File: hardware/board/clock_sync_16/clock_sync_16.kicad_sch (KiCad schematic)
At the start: 1 part, among them U21 SN74LVC1G125DCK

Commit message: route pcb v0.1
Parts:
- added C10: 1uF, Capacitor_SMD:C_0402_1005Metric, symbol Device:C
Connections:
- net +3.3V: now also C10.1
- net GND: now also C10.2
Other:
- note removed: "TODO: Ephys "slow uart" output. TODO: 32.768KHz crystal."
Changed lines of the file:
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@@
     (company "The Allen Institute")
   )
+  (wire (pts (xy 140.335 189.23) (xy 140.335 190.5))
+    (stroke (width 0) (type default))
+  )
   (wire (pts (xy 155.575 48.26) (xy 156.845 48.26))
     (stroke (width 0) (type default))
@@
     (stroke (width 0) (type default))
   )
+  (wire (pts (xy 140.335 180.34) (xy 140.335 181.61))
+    (stroke (width 0) (type default))
+  )
   (wire (pts (xy 142.875 36.83) (xy 142.875 38.1))
     (stroke (width 0) (type default))
@@
   (wire (pts (xy 105.41 76.2) (xy 181.61 76.2))
     (stroke (width 0) (type default))
-  )
-  (text "TODO: Ephys \"slow uart\" output.\nTODO: 32.768KHz crystal."
-    (at 123.19 146.685 0)
-    (effects (font (size 2 2) (thickness 0.4) bold) (justify left bottom))
   )
   (global_label "HARP_CLKOUT" (shape input) (at 156.845 48.26 0) (fields_autoplaced)
@@
     )
   )
+  (symbol (lib_id "Device:C") (at 140.335 185.42 0) (unit 1)
+    (in_bom yes) (on_board yes) (dnp no)
+    (property "Reference" "C10" (at 140.335 182.88 0)
+      (effects (font (size 1.27 1.27)) (justify left))
+    )
+    (property "Value" "1uF" (at 141.605 187.96 0)
+      (effects (font (size 1.27 1.27)) (justify left))
+    )
+    (property "Footprint" "Capacitor_SMD:C_0402_1005Metric" (at 141.3002 189.23 0)
+      (effects (font (size 1.27 1.27)) hide)
+    )
+    (property "Datasheet" "https://search.murata.co.jp/Ceramy/image/img/A01X/G101/ENG/GRM155R6YA105KE11-01.pdf" (at 140.335 185.42 0)
+      (effects (font (size 1.27 1.27)) hide)
+    )
+    (property "Notes" "must not be polarized" (at 140.335 185.42 0)
+      (effects (font (size 1.27 1.27)) hide)
+    )
+    (property "Link" "https://www.digikey.com/en/products/detail/murata-electronics/GRM155R6YA105KE11J/4905163" (at 140.335 185.42 0)
+      (effects (font (size 1.27 1.27)) hide)
+    )
+    (property "Manufacturer Number" "GRM155R6YA105KE11J" (at 140.335 185.42 0)
+      (effects (font (size 1.27 1.27)) hide)
+    )
+    (property "Manufacturer" "Murata Electronics" (at 140.335 185.42 0)
+      (effects (font (size 1.27 1.27)) hide)
+    )
+    (property "Rated Voltage" "35V" (at 140.335 185.42 0)
+      (effects (font (size 1.27 1.27)) hide)
+    )
+    (property "Temperature Coefficient" "X5R" (at 140.335 185.42 0)
+      (effects (font (size 1.27 1.27)) hide)
+    )
+    (property "PCBWay Link" "" (at 140.335 185.42 0)
+      (effects (font (size 1.27 1.27)) hide)
+    )
+    (pin "1")
+    (pin "2")
+    (instances
+      (project "clock_sync_16"
+        (path "/8fe3245e-7a82-4862-8bfd-ddbb03ffdc18/ba147b73-594a-4106-8069-105093132ec6"
+          (reference "C10") (unit 1)
+        )
+        (path "/8fe3245e-7a82-4862-8bfd-ddbb03ffdc18"
+          (reference "C54") (unit 1)
+        )
+      )
+      (project "harp_lick_detector_capactive"
+        (path "/e63e39d7-6ac0-4ffd-8aa3-1841a4541b55/eb8325ca-9747-4676-8e08-1fb825a7219f"
+          (reference "C8") (unit 1)
+        )
+      )
+    )
+  )
+  (symbol (lib_id "power:+3.3V") (at 140.335 180.34 0) (unit 1)
+    (in_bom yes) (on_board yes) (dnp no)
+    (property "Reference" "#PWR09" (at 140.335 184.15 0)
+      (effects (font (size 1.27 1.27)) hide)
+    )
+    (property "Value" "+3.3V" (at 140.335 176.53 0)
+      (effects (font (size 1.27 1.27)))
+    )
+    (property "Footprint" "" (at 140.335 180.34 0)
+      (effects (font (size 1.27 1.27)) hide)
+    )
+    (property "Datasheet" "" (at 140.335 180.34 0)
+      (effects (font (size 1.27 1.27)) hide)
+    )
+    (pin "1")
+    (instances
+      (project "clock_sync_16"
+        (path "/8fe3245e-7a82-4862-8bfd-ddbb03ffdc18/ba147b73-594a-4106-8069-105093132ec6"
+          (reference "#PWR09") (unit 1)
+        )
+        (path "/8fe3245e-7a82-4862-8bfd-ddbb03ffdc18"
+          (reference "#PWR037") (unit 1)
+        )
+      )
+    )
+  )
   (symbol (lib_id "74xGxx:SN74LVC1G125DCK") (at 142.875 48.26 0) (unit 1)
     (in_bom yes) (on_board yes) (dnp no)
@@
     )
   )
-  (symbol (lib_name "+3.3V_1") (lib_id "power:+3.3V") (at 137.795 36.83 0) (unit 1)
+  (symbol (lib_id "power:GND") (at 140.335 190.5 0) (unit 1)
+    (in_bom yes) (on_board yes) (dnp no)
+    (property "Reference" "#PWR058" (at 140.335 196.85 0)
+      (effects (font (size 1.27 1.27)) hide)
+    )
+    (property "Value" "GND" (at 140.335 194.31 0)
+      (effects (font (size 1.27 1.27)))
+    )
+    (property "Footprint" "" (at 140.335 190.5 0)
+      (effects (font (size 1.27 1.27)) hide)
+    )
+    (property "Datasheet" "" (at 140.335 190.5 0)
+      (effects (font (size 1.27 1.27)) hide)
+    )
+    (pin "1")
+    (instances
+      (project "clock_sync_16"
+        (path "/8fe3245e-7a82-4862-8bfd-ddbb03ffdc18"
+          (reference "#PWR058") (unit 1)
+        )
+      )
+    )
+  )
+  (symbol (lib_id "power:+3.3V") (at 137.795 36.83 0) (unit 1)
     (in_bom yes) (on_board yes) (dnp no)
     (property "Reference" "#PWR09" (at 137.795 40.64 0)

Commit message: draft v0.1 pcb
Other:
- note added: "Buffer Bypass Cap"
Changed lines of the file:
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@@
     (stroke (width 0) (type default))
+  )
+  (text "Buffer Bypass Cap" (at 133.35 173.355 0)
+    (effects (font (size 1.27 1.27)) (justify left bottom))
   )
   (global_label "HARP_CLKOUT" (shape input) (at 156.845 48.26 0) (fields_autoplaced)

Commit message: draft firmware
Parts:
- U21: Manufacturer (none) -> Texas Instruments; Manufacturer Number (none) -> SN74LVC1G125DCKR
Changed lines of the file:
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@@
+      (effects (font (size 1.27 1.27)) hide)
+    )
+    (property "Manufacturer" "Texas Instruments" (at 142.875 48.26 0)
+      (effects (font (size 1.27 1.27)) hide)
+    )
+    (property "Manufacturer Number" "SN74LVC1G125DCKR" (at 142.875 48.26 0)
       (effects (font (size 1.27 1.27)) hide)
     )

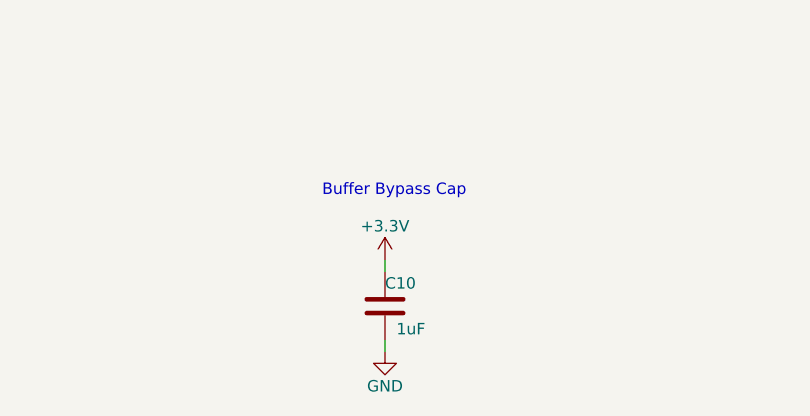
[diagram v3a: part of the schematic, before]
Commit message: add pps/slow_uart output options
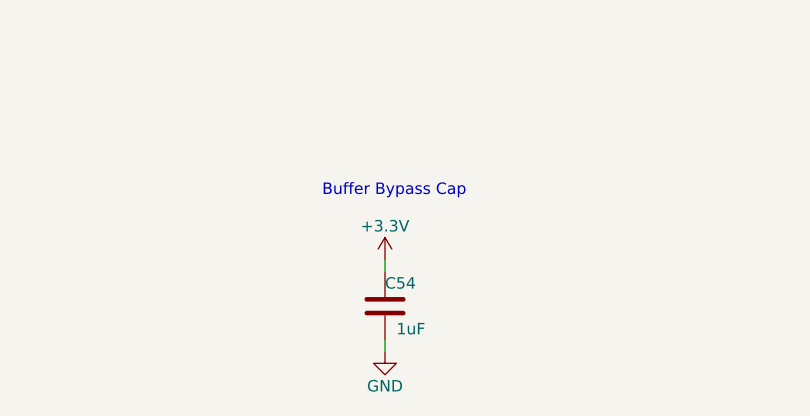
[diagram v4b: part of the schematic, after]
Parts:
- renumbered C10 to C54

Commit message: update harp core; update led resistors and deprecated parts; bump versions
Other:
- title: (none) -> harp.device.white-rabbit
- moved on the sheet: C54
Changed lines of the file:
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@@
 	(paper "A4")
 	(title_block
-		(rev "0.1")
+		(title "harp.device.white-rabbit")
+		(date "2025-02-21")
+		(rev "1.0.0")
 		(company "The Allen Institute")
 	)
 	(wire
 		(pts
-			(xy 140.335 189.23) (xy 140.335 190.5)
+			(xy 162.56 189.23) (xy 162.56 190.5)
 		)
 		(stroke
@@
 	(wire
 		(pts
-			(xy 140.335 180.34) (xy 140.335 181.61)
+			(xy 162.56 180.34) (xy 162.56 181.61)
 		)
 		(stroke
@@
 	(text "Buffer Bypass Cap"
 		(exclude_from_sim no)
-		(at 133.35 173.355 0)
+		(at 154.94 172.72 0)
 		(effects
 			(font
@@
 	(symbol
 		(lib_id "Device:C")
-		(at 140.335 185.42 0)
+		(at 162.56 185.42 0)
 		(unit 1)
 		(exclude_from_sim no)
@@
 		(dnp no)
 		(property "Reference" "C54"
-			(at 140.335 182.88 0)
+			(at 162.56 182.88 0)
 			(effects
 				(font
@@
 		)
 		(property "Value" "1uF"
-			(at 141.605 187.96 0)
+			(at 163.83 187.96 0)
 			(effects
 				(font
@@
 		)
 		(property "Footprint" "Capacitor_SMD:C_0402_1005Metric"
-			(at 141.3002 189.23 0)
+			(at 163.5252 189.23 0)
 			(effects
 				(font
@@
 		)
 		(property "Datasheet" "https://search.murata.co.jp/Ceramy/image/img/A01X/G101/ENG/GRM155R6YA105KE11-01.pdf"
-			(at 140.335 185.42 0)
+			(at 162.56 185.42 0)
 			(effects
 				(font
@@
 		)
 		(property "Description" ""
-			(at 140.335 185.42 0)
+			(at 162.56 185.42 0)
 			(effects
 				(font
@@
 		)
 		(property "Notes" "must not be polarized"
-			(at 140.335 185.42 0)
+			(at 162.56 185.42 0)
 			(effects
 				(font
@@
 		)
 		(property "Link" "https://www.digikey.com/en/products/detail/murata-electronics/GRM155R6YA105KE11J/4905163"
-			(at 140.335 185.42 0)
+			(at 162.56 185.42 0)
 			(effects
 				(font
@@
 		)
 		(property "Manufacturer Number" "GRM155R6YA105KE11J"
-			(at 140.335 185.42 0)
+			(at 162.56 185.42 0)
 			(effects
 				(font
@@
 		)
 		(property "Manufacturer" "Murata Electronics"
-			(at 140.335 185.42 0)
+			(at 162.56 185.42 0)
 			(effects
 				(font
@@
 		)
 		(property "Rated Voltage" "35V"
-			(at 140.335 185.42 0)
+			(at 162.56 185.42 0)
 			(effects
 				(font
@@
 		)
 		(property "Temperature Coefficient" "X5R"
-			(at 140.335 185.42 0)
+			(at 162.56 185.42 0)
 			(effects
 				(font
@@
 		)
 		(property "PCBWay Link" ""
-			(at 140.335 185.42 0)
+			(at 162.56 185.42 0)
 			(effects
 				(font
@@
 	(symbol
 		(lib_id "power:+3.3V")
-		(at 140.335 180.34 0)
+		(at 162.56 180.34 0)
 		(unit 1)
 		(exclude_from_sim no)
@@
 		(dnp no)
 		(property "Reference" "#PWR037"
-			(at 140.335 184.15 0)
+			(at 162.56 184.15 0)
 			(effects
 				(font
@@
 		)
 		(property "Value" "+3.3V"
-			(at 140.335 176.53 0)
+			(at 162.56 176.53 0)
 			(effects
 				(font
@@
 		)
 		(property "Footprint" ""
-			(at 140.335 180.34 0)
+			(at 162.56 180.34 0)
 			(effects
 				(font
@@
 		)
 		(property "Datasheet" ""
-			(at 140.335 180.34 0)
+			(at 162.56 180.34 0)
 			(effects
 				(font
@@
 		)
 		(property "Description" ""
-			(at 140.335 180.34 0)
+			(at 162.56 180.34 0)
 			(effects
 				(font
@@
 	(symbol
 		(lib_id "power:GND")
-		(at 140.335 190.5 0)
+		(at 162.56 190.5 0)
 		(unit 1)
 		(exclude_from_sim no)
@@
 		(dnp no)
 		(property "Reference" "#PWR058"
-			(at 140.335 196.85 0)
+			(at 162.56 196.85 0)
 			(effects
 				(font
@@
 		)
 		(property "Value" "GND"
-			(at 140.335 194.31 0)
+			(at 162.56 194.31 0)
 			(effects
 				(font
@@
 		)
 		(property "Footprint" ""
-			(at 140.335 190.5 0)
+			(at 162.56 190.5 0)
 			(effects
 				(font
@@
 		)
 		(property "Datasheet" ""
-			(at 140.335 190.5 0)
+			(at 162.56 190.5 0)
 			(effects
 				(font
@@
 		)
 		(property "Description" ""
-			(at 140.335 190.5 0)
-			(effects
-				(font
+			(at 162.56 190.5 0)
+			(effects
+				(font
